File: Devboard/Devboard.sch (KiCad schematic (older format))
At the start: 23 parts, among them J1 9V DC, J2 In 3.5mm, J3 In 6.3mm, J4 Out 3.5mm, J5 Out 6.3mm, J6 I/O, U1 TL074

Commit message: New Devboard iteration
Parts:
- removed C2: 10uF, Capacitor_THT:CP_Radial_D5.0mm_P2.00mm, symbol Device:CP1
- removed J2: In 3.5mm, Connector_Audio:Jack_3.5mm_Ledino_KB3SPRS_Horizontal, symbol Connector:AudioJack2
- removed J3: In 6.3mm, Connector_Audio:Jack_6.35mm_Neutrik_NMJ6HFD4_Horizontal, symbol Connector:AudioJack2
- removed J4: Out 3.5mm, Connector_Audio:Jack_3.5mm_Ledino_KB3SPRS_Horizontal, symbol Connector:AudioJack2
- removed J5: Out 6.3mm, Connector_Audio:Jack_6.35mm_Neutrik_NMJ6HFD4_Horizontal, symbol Connector:AudioJack2
- removed R6, R7: 1k, Resistor_THT:R_Axial_DIN0207_L6.3mm_D2.5mm_P10.16mm_Horizontal, symbol Device:R
- removed unit 2 of U1
- added C1: 1uF, symbol Device:C
- added C10, C11, C12, C13, C14, C15: 10nF, symbol Device:C
- added C6: 10uF, symbol Device:CP1
- added C9: 100nF, Capacitor_THT:C_Rect_L9.0mm_W2.5mm_P7.50mm_MKT, symbol Device:C
- added D10, D11, D12, D13, D14, D15, D16, D17, D18, D2, D3, D5, D6, D7, D8, D9: 1N4148, symbol Device:D
- added D4: Power, symbol Device:LED
- added J2: In 3.5mm, symbol Connector:AudioJack3_Switch
- added J3: In 6.3mm, symbol Connector:AudioJack3_Switch
- added J4: Out 3.5mm, symbol Connector:AudioJack3_Switch
- added J5: Out 6.3mm, symbol Connector:AudioJack3_Switch
- added J7: Power In, symbol Connector:Conn_01x03_Male
- added J8: Power Out, symbol Connector:Conn_01x03_Male
- added R1: 10k, Resistor_THT:R_Axial_DIN0207_L6.3mm_D2.5mm_P10.16mm_Horizontal, symbol Device:R
- added R10: 1M, Resistor_THT:R_Axial_DIN0207_L6.3mm_D2.5mm_P10.16mm_Horizontal, symbol Device:R
- added R2: 100, Resistor_THT:R_Axial_DIN0207_L6.3mm_D2.5mm_P10.16mm_Horizontal, symbol Device:R
- added R3: 1k, symbol Device:R
- added RV1, RV2: A50k, symbol Device:R_POT
- added SW1: On/Off, symbol Switch:SW_SPST
- added SW2: Output Clipping, symbol Switch:SW_SPST
- added SW3: Input Clipping, symbol Switch:SW_SPST
- added unit 3 of U1
- added U2: NE5532, symbol Amplifier_Operational:NE5532
- C7: footprint Capacitor_THT:CP_Radial_D5.0mm_P2.00mm -> (none)
- D1: value 1N4148 -> 1N5817
- R6: renamed from R3; value 100k -> 1M
- R7: renamed from R4; value 1k -> 10k
- R8: renamed from R5; value 1k -> 100
- R9: renamed from R8; value 100k -> 1M
- renumbered C1 to C2, C6 to C8, R1 to R4, R2 to R5
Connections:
- wire segments 70 -> 129
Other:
- note added: "Input Gain"
- note added: "Output Gain"
- note removed: "TODO: Input / Output gain"
- note removed: "TODO: Power switch"
- moved on the sheet: C2, C3, C4, C5, C8, J6, R4, R5, R6, R7, R8, R9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

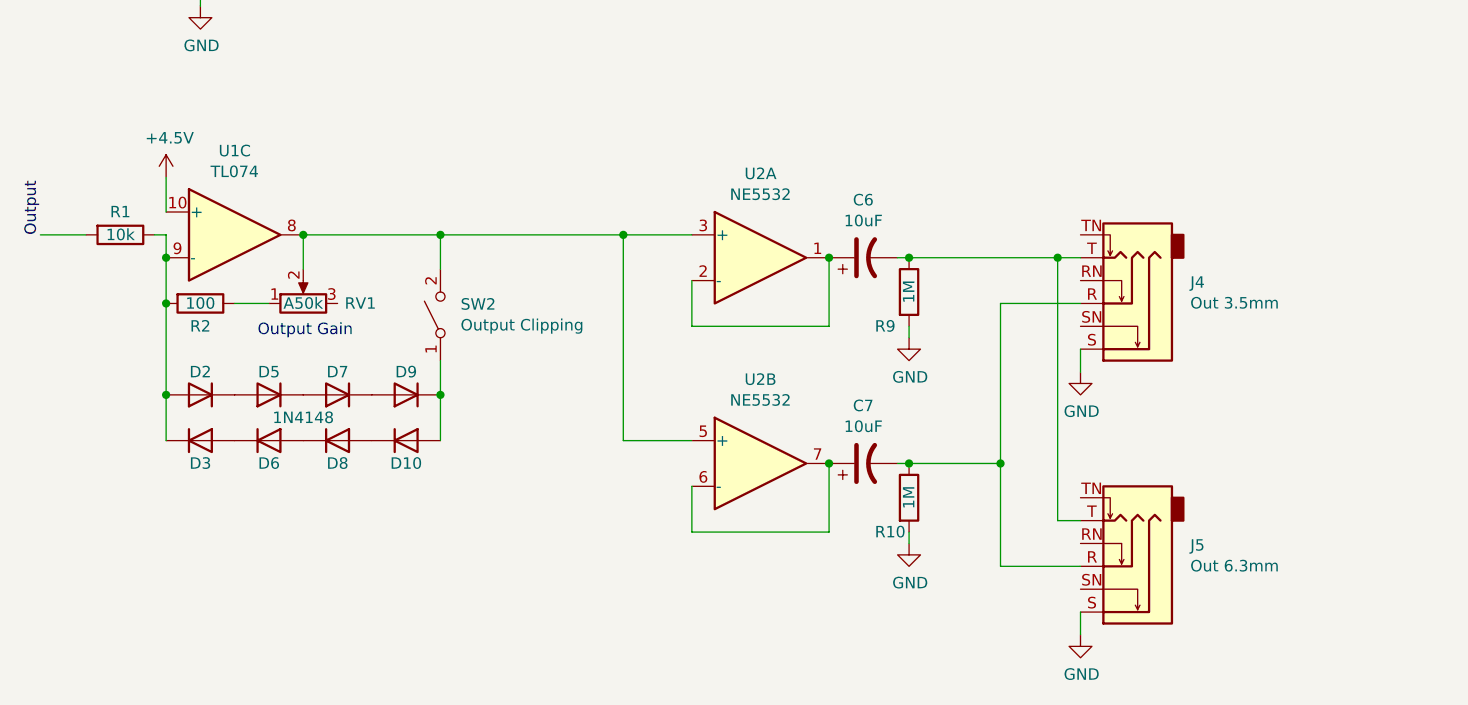
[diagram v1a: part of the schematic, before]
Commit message: New Devboard iteration, get rid of output clipping and limit gain to unity
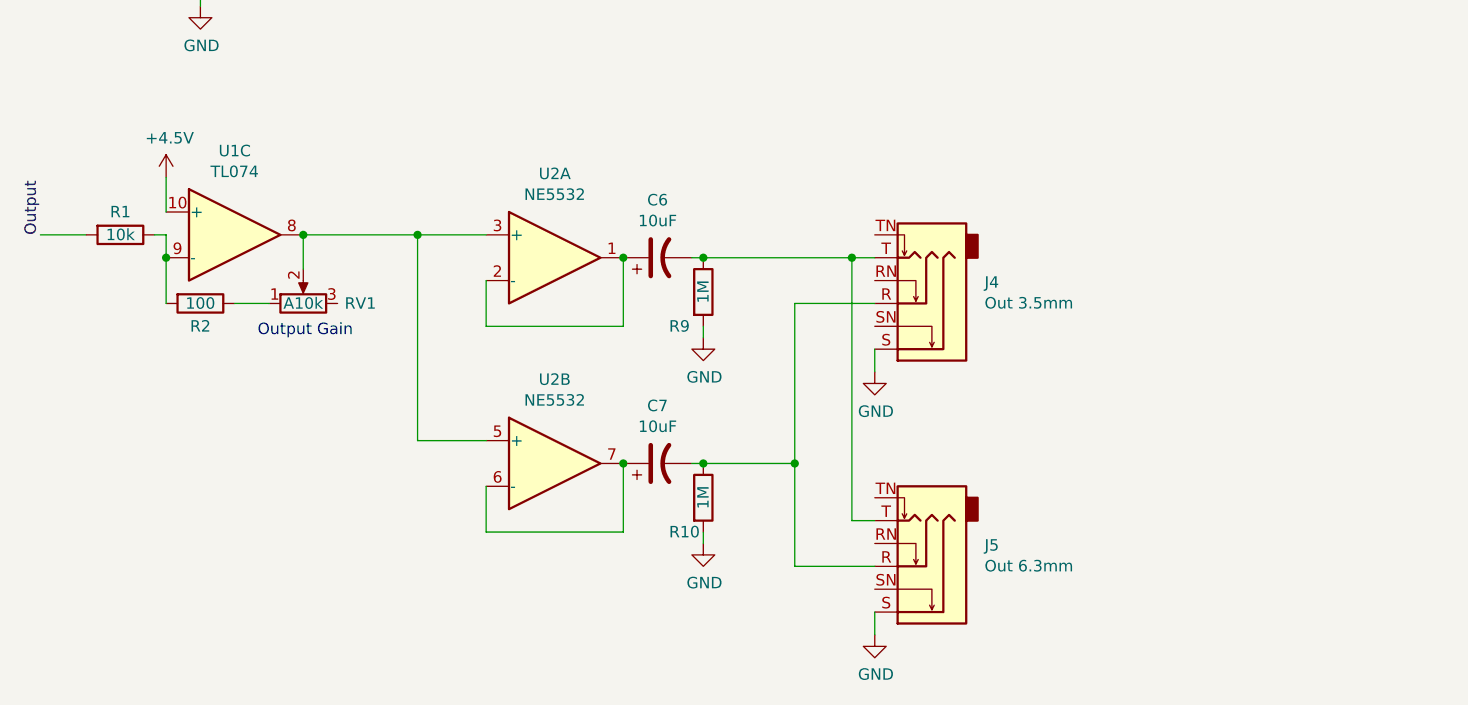
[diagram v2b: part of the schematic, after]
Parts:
- removed D10, D2, D3, D5, D6, D7, D8, D9: 1N4148, symbol Device:D
- removed SW2: Output Clipping, symbol Switch:SW_SPST
- RV1: value A50k -> A10k
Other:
- moved on the sheet: C6, C7, J4, J5, R10, R9, U2A, U2B
